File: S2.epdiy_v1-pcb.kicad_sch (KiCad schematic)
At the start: 93 parts, among them J1 USB_C_Receptacle_USB2.0, J2 Jack-DC, P1 CONN_02X13, Q1 MMBT3904, Q2 MMBT3904, SW1 RESET, SW2 BOOT, U1 MCP1700-1202E_SOT23, U11 TP4056, U2 ESP32-S2-WROVER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

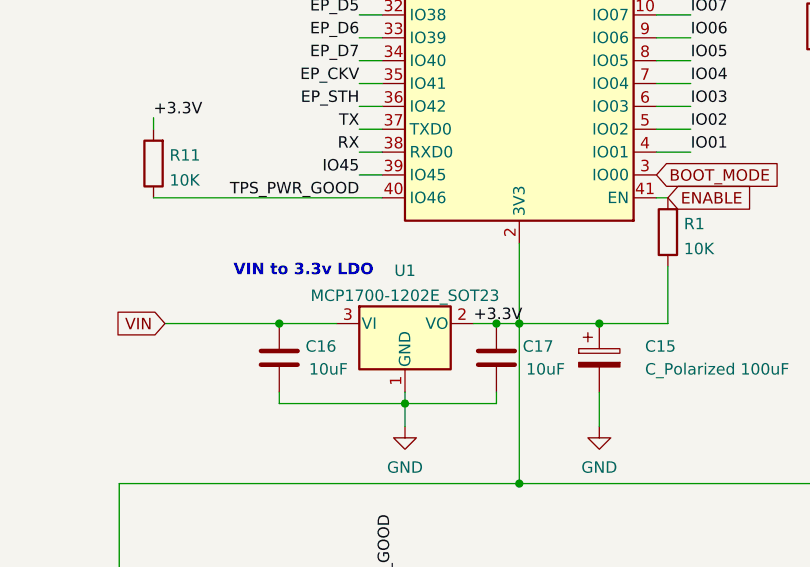
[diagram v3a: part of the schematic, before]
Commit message: Update with right LDO 3.3V
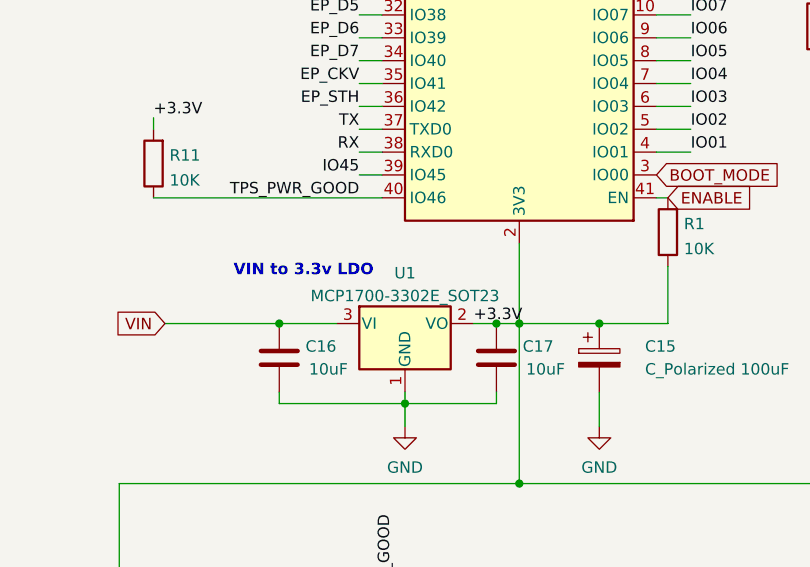
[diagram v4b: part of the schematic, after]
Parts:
- U1: value MCP1700-1202E_SOT23 -> MCP1700-3302E_SOT23; LCSC (none) -> C39051
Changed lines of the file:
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@@
   (symbol (lib_id "Regulator_Linear:MCP1700-1202E_SOT23") (at 119.38 105.41 0) (unit 1)
     (in_bom yes) (on_board yes) (fields_autoplaced)
-    (property "Reference" "U1" (id 0) (at 119.38 99.5385 0))
-    (property "Value" "MCP1700-1202E_SOT23" (id 1) (at 119.38 102.3136 0))
+    (property "Reference" "U1" (id 0) (at 119.38 99.8052 0))
+    (property "Value" "MCP1700-3302E_SOT23" (id 1) (at 119.38 102.3421 0))
     (property "Footprint" "Package_TO_SOT_SMD:SOT-23" (id 2) (at 119.38 99.695 0)
       (effects (font (size 1.27 1.27)) hide)
     )
     (property "Datasheet" "http://ww1.microchip.com/downloads/en/DeviceDoc/20001826D.pdf" (id 3) (at 119.38 105.41 0)
+      (effects (font (size 1.27 1.27)) hide)
+    )
+    (property "LCSC" "C39051" (id 4) (at 119.38 105.41 0)
       (effects (font (size 1.27 1.27)) hide)
     )
@@
     )
     (path "/6f2dad6e-4f7a-4655-bd41-70ba0551820e"
-      (reference "U1") (unit 1) (value "MCP1700-1202E_SOT23") (footprint "Package_TO_SOT_SMD:SOT-23")
+      (reference "U1") (unit 1) (value "MCP1700-3302E_SOT23") (footprint "Package_TO_SOT_SMD:SOT-23")
     )
     (path "/68b01932-f792-42f5-89bd-ba00765e8d21"

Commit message: New 1.1 design
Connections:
- net DTR: now also P1.20 (Pin_20); no longer P1.21 (Pin_21)
- net RTS: now also P1.22 (Pin_22)
- net RX: now also P1.24 (Pin_24); no longer P1.23 (Pin_23)
- net SCL: now also P1.14 (Pin_14); no longer P1.18 (Pin_18)
- net SDA: now also P1.16 (Pin_16); no longer P1.20 (Pin_20)
- net TPS_PWR_GOOD: no longer P1.26 (Pin_26)
- net TX: now also P1.26 (Pin_26); no longer P1.25 (Pin_25)
- net RST: no longer names the net of P1.19 (Pin_19)
- no-connect marks 18 -> 19

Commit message: Production files REV 1.1
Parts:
- C2, C22, C3: LCSC (none) -> C49678
- C38: value 1uF/25V -> (none); footprint Capacitor_SMD:C_0805_2012Metric -> (none)
- J1: value USB_C_Receptacle_USB2.0 -> (none); footprint footprint:USB_C_Receptacle_HRO_TYPE-C-31-M-12 -> (none)
- L1: value 4.7uH -> (none); footprint Inductor_SMD:L_Taiyo-Yuden_NR-50xx_HandSoldering -> (none); LCSC C222947 -> C222947
- L2: value 2.2uH -> (none); footprint Inductor_SMD:L_Taiyo-Yuden_NR-40xx_HandSoldering -> (none)
- R1, R11, R12, R13, R14, R8: LCSC (none) -> C25197
- R10, R9: LCSC (none) -> C4190
- R18: value 43k -> (none); footprint Resistor_SMD:R_0603_1608Metric -> (none)
- R28: value 47k -> (none); footprint Resistor_SMD:R_0603_1608Metric -> (none)
- R4: value 400 -> (none); footprint Resistor_SMD:R_0603_1608Metric -> (none); LCSC (none) -> C23151
- R5: LCSC (none) -> C23212
- TH1: value 10k/3380K -> (none); footprint Resistor_SMD:R_0603_1608Metric -> (none)
- U11: value TP4056 -> (none); footprint TP4056:TP4056_SOP-8-PP -> (none)
- U2: value ESP32-S2-WROVER -> (none); footprint RF_Module:ESP32-S2-WROVER -> (none)
- U6: value ED060XC5 -> (none); footprint footprint:X05A20H34G -> (none)
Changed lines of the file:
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@@
     (in_bom yes) (on_board yes)
     (property "Reference" "L2" (id 0) (at 335.28 173.2026 90))
-    (property "Value" "2.2uH" (id 1) (at 335.28 175.514 90))
-    (property "Footprint" "Inductor_SMD:L_Taiyo-Yuden_NR-40xx_HandSoldering" (id 2) (at 335.28 177.8 0)
+    (property "Value" "" (id 1) (at 335.28 175.514 90))
+    (property "Footprint" "" (id 2) (at 335.28 177.8 0)
       (effects (font (size 1.27 1.27)) hide)
     )
@@
       (effects (font (size 1.27 1.27)) (justify left))
     )
-    (property "Value" "ED060XC5" (id 1) (at 80.7212 232.283 0)
-      (effects (font (size 1.27 1.27)) (justify left))
-    )
-    (property "Footprint" "footprint:X05A20H34G" (id 2) (at 67.31 184.15 0)
+    (property "Value" "" (id 1) (at 80.7212 232.283 0)
+      (effects (font (size 1.27 1.27)) (justify left))
+    )
+    (property "Footprint" "" (id 2) (at 67.31 184.15 0)
       (effects (font (size 1.27 1.27)) hide)
     )
@@
       (effects (font (size 1.27 1.27)) (justify right))
     )
-    (property "Value" "10k/3380K" (id 1) (at 323.9008 153.543 0)
-      (effects (font (size 1.27 1.27)) (justify right))
-    )
-    (property "Footprint" "Resistor_SMD:R_0603_1608Metric" (id 2) (at 320.04 153.67 0)
+    (property "Value" "" (id 1) (at 323.9008 153.543 0)
+      (effects (font (size 1.27 1.27)) (justify right))
+    )
+    (property "Footprint" "" (id 2) (at 320.04 153.67 0)
       (effects (font (size 1.27 1.27)) hide)
     )
@@
       (effects (font (size 1.27 1.27)) (justify left))
     )
-    (property "Value" "43k" (id 1) (at 315.468 153.543 0)
-      (effects (font (size 1.27 1.27)) (justify left))
-    )
-    (property "Footprint" "Resistor_SMD:R_0603_1608Metric" (id 2) (at 311.912 152.4 90)
+    (property "Value" "" (id 1) (at 315.468 153.543 0)
+      (effects (font (size 1.27 1.27)) (justify left))
+    )
+    (property "Footprint" "" (id 2) (at 311.912 152.4 90)
       (effects (font (size 1.27 1.27)) hide)
     )
@@
     (in_bom yes) (on_board yes)
     (property "Reference" "L1" (id 0) (at 298.9326 222.25 90))
-    (property "Value" "4.7uH" (id 1) (at 301.244 222.25 90))
-    (property "Footprint" "Inductor_SMD:L_Taiyo-Yuden_NR-50xx_HandSoldering" (id 2) (at 303.53 222.25 0)
+    (property "Value" "" (id 1) (at 301.244 222.25 90))
+    (property "Footprint" "" (id 2) (at 303.53 222.25 0)
       (effects (font (size 1.27 1.27)) hide)
     )
@@
       (effects (font (size 1.27 1.27)) hide)
     )
-    (property "LCSC" " C222947" (id 4) (at 303.53 222.25 90)
+    (property "LCSC" "C222947" (id 4) (at 303.53 222.25 90)
       (effects (font (size 1.27 1.27)) hide)
     )
@@
       (effects (font (size 1.27 1.27)) (justify left))
     )
-    (property "Value" "47k" (id 1) (at 146.558 215.773 0)
-      (effects (font (size 1.27 1.27)) (justify left))
-    )
-    (property "Footprint" "Resistor_SMD:R_0603_1608Metric" (id 2) (at 143.002 214.63 90)
+    (property "Value" "" (id 1) (at 146.558 215.773 0)
+      (effects (font (size 1.27 1.27)) (justify left))
+    )
+    (property "Footprint" "" (id 2) (at 143.002 214.63 90)
       (effects (font (size 1.27 1.27)) hide)
     )
@@
       (effects (font (size 1.27 1.27)) (justify left))
     )
-    (property "Value" "1uF/25V" (id 1) (at 165.481 241.173 0)
-      (effects (font (size 1.27 1.27)) (justify left))
-    )
-    (property "Footprint" "Capacitor_SMD:C_0805_2012Metric" (id 2) (at 163.5252 243.84 0)
+    (property "Value" "" (id 1) (at 165.481 241.173 0)
+      (effects (font (size 1.27 1.27)) (justify left))
+    )
+    (property "Footprint" "" (id 2) (at 163.5252 243.84 0)
       (effects (font (size 1.27 1.27)) hide)
     )
@@
     )
     (property "Datasheet" "~" (id 3) (at 171.45 69.85 0)
+      (effects (font (size 1.27 1.27)) hide)
+    )
+    (property "LCSC" "C4190" (id 4) (at 171.45 69.85 0)
       (effects (font (size 1.27 1.27)) hide)
     )
@@
       (effects (font (size 1.27 1.27)) hide)
     )
+    (property "LCSC" "C25197" (id 4) (at 223.52 58.42 90)
+      (effects (font (size 1.27 1.27)) hide)
+    )
     (pin "1")
     (pin "2")
@@
     )
     (property "Datasheet" "~" (id 3) (at 173.99 57.15 0)
+      (effects (font (size 1.27 1.27)) hide)
+    )
+    (property "LCSC" "C25197" (id 4) (at 173.99 57.15 0)
       (effects (font (size 1.27 1.27)) hide)
     )
@@
       (effects (font (size 1.27 1.27)) hide)
     )
+    (property "LCSC" " C49678" (id 4) (at 331.47 53.34 0)
+      (effects (font (size 1.27 1.27)) hide)
+    )
     (pin "1")
     (pin "2")
@@
       (effects (font (size 1.27 1.27)) (justify left))
     )
-    (property "Value" "400" (id 1) (at 343.408 57.7466 0)
-      (effects (font (size 1.27 1.27)) (justify left))
-    )
-    (property "Footprint" "Resistor_SMD:R_0603_1608Metric" (id 2) (at 339.852 55.88 90)
+    (property "Value" "" (id 1) (at 343.408 57.7466 0)
+      (effects (font (size 1.27 1.27)) (justify left))
+    )
+    (property "Footprint" "" (id 2) (at 339.852 55.88 90)
       (effects (font (size 1.27 1.27)) hide)
     )
@@
       (effects (font (size 1.27 1.27)) hide)
     )
+    (property "LCSC" "C23151" (id 4) (at 341.63 55.88 0)
+      (effects (font (size 1.27 1.27)) hide)
+    )
     (pin "1")
     (pin "2")
@@
     )
     (property "Datasheet" "~" (id 3) (at 374.65 92.71 0)
+      (effects (font (size 1.27 1.27)) hide)
+    )
+    (property "LCSC" "C23212" (id 4) (at 374.65 92.71 0)
       (effects (font (size 1.27 1.27)) hide)
     )
@@
       (effects (font (size 1.27 1.27)) (justify right))
     )
-    (property "Value" "ESP32-S2-WROVER" (id 1) (at 132.6006 39.4486 0)
-      (effects (font (size 1.27 1.27)) (justify right))
-    )
-    (property "Footprint" "RF_Module:ESP32-S2-WROVER" (id 2) (at 113.03 36.83 0)
+    (property "Value" "" (id 1) (at 132.6006 39.4486 0)
+      (effects (font (size 1.27 1.27)) (justify right))
+    )
+    (property "Footprint" "" (id 2) (at 113.03 36.83 0)
       (effects (font (size 1.27 1.27)) hide)
     )
@@
       (effects (font (size 1.27 1.27)) hide)
     )
+    (property "LCSC" "C25197" (id 4) (at 91.44 87.63 0)
+      (effects (font (size 1.27 1.27)) hide)
+    )
     (pin "1")
     (pin "2")
@@
       (effects (font (size 1.27 1.27)) hide)
     )
+    (property "LCSC" "C25197" (id 4) (at 186.69 45.72 0)
+      (effects (font (size 1.27 1.27)) hide)
+    )
     (pin "1")
     (pin "2")
@@
     (in_bom yes) (on_board yes) (fields_autoplaced)
     (property "Reference" "J1" (id 0) (at 60.96 29.0535 0))
-    (property "Value" "USB_C_Receptacle_USB2.0" (id 1) (at 60.96 31.8286 0))
-    (property "Footprint" "footprint:USB_C_Receptacle_HRO_TYPE-C-31-M-12" (id 2) (at 64.77 50.8 0)
+    (property "Value" "" (id 1) (at 60.96 31.8286 0))
+    (property "Footprint" "" (id 2) (at 64.77 50.8 0)
       (effects (font (size 1.27 1.27)) hide)
     )
@@
       (effects (font (size 1.27 1.27)) hide)
     )
+    (property "LCSC" "C4190" (id 4) (at 165.1 72.39 0)
+      (effects (font (size 1.27 1.27)) hide)
+    )
     (pin "1")
     (pin "2")
@@
     )
     (property "Datasheet" "~" (id 3) (at 325.12 53.34 0)
+      (effects (font (size 1.27 1.27)) hide)
+    )
+    (property "LCSC" " C49678" (id 4) (at 325.12 53.34 0)
       (effects (font (size 1.27 1.27)) hide)
     )
@@
       (effects (font (size 1.27 1.27)) hide)
     )
+    (property "LCSC" "C25197" (id 4) (at 223.52 74.93 90)
+      (effects (font (size 1.27 1.27)) hide)
+    )
     (pin "1")
     (pin "2")
@@
       (effects (font (size 1.524 1.524)))
     )
-    (property "Value" "TP4056" (id 1) (at 361.95 75.0751 0)
+    (property "Value" "" (id 1) (at 361.95 75.0751 0)
       (effects (font (size 1.524 1.524)))
     )
-    (property "Footprint" "TP4056:TP4056_SOP-8-PP" (id 2) (at 361.95 75.0751 0)
+    (property "Footprint" "" (id 2) (at 361.95 75.0751 0)
       (effects (font (size 1.524 1.524)) hide)
     )
@@
       (effects (font (size 1.27 1.27)) hide)
     )
+    (property "LCSC" "C25197" (id 4) (at 148.59 95.25 0)
+      (effects (font (size 1.27 1.27)) hide)
+    )
     (pin "1")
     (pin "2")
@@
       (effects (font (size 1.27 1.27)) hide)
     )
+    (property "LCSC" " C49678" (id 4) (at 374.65 82.55 0)
+      (effects (font (size 1.27 1.27)) hide)
+    )
